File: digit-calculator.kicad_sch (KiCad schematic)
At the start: 4 parts, among them J1 Trackball, SW1 SW_SPST, U1 XIAO-ESP32-C3-SMD

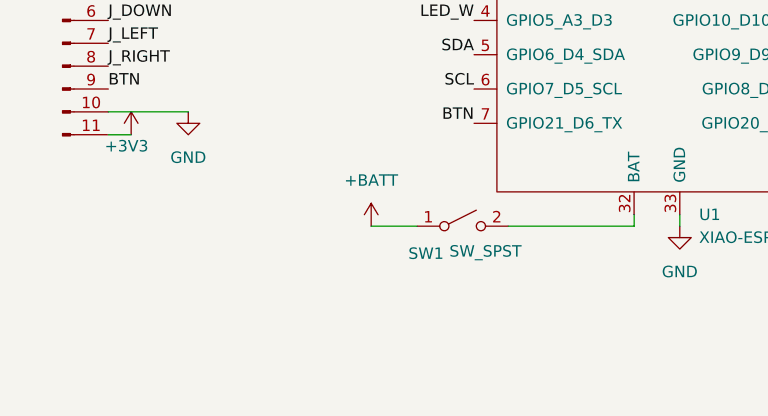
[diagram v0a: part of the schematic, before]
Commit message: Add battery connector
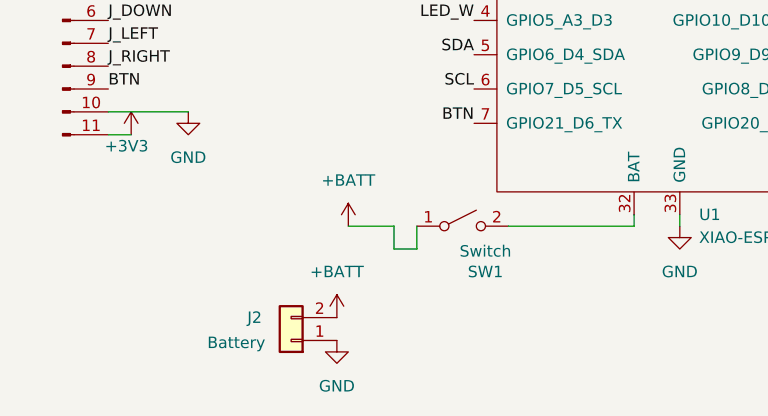
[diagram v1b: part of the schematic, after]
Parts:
- added J2: Battery, symbol Connector_Generic:Conn_01x02
- Brd1: footprint Display:SSD1306-OLED -> Display:SSD1306-0.91-OLED-4pin-128x32
- SW1: value SW_SPST -> Switch
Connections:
- net +BATT: now also J2.2 (Pin_2)
- net GND: now also J2.1 (Pin_1)
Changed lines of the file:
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@@
+	(wire
+		(pts
+			(xy 111.76 115.57) (xy 114.3 115.57)
+		)
+		(stroke
+			(width 0)
+			(type default)
+		)
+	)
+	(wire
+		(pts
+			(xy 111.76 113.03) (xy 111.76 115.57)
+		)
+		(stroke
+			(width 0)
+			(type default)
+		)
+	)
 	(wire
 		(pts
@@
 	(wire
 		(pts
-			(xy 109.22 113.03) (xy 114.3 113.03)
+			(xy 114.3 115.57) (xy 114.3 113.03)
 		)
 		(stroke
@@
 	(wire
 		(pts
-			(xy 124.46 113.03) (xy 138.43 113.03)
+			(xy 106.68 113.03) (xy 111.76 113.03)
 		)
 		(stroke
@@
 	(wire
 		(pts
-			(xy 138.43 113.03) (xy 138.43 111.76)
+			(xy 124.46 113.03) (xy 138.43 113.03)
 		)
 		(stroke
@@
 	(wire
 		(pts
-			(xy 162.56 86.36) (xy 170.18 86.36)
+			(xy 138.43 113.03) (xy 138.43 111.76)
 		)
 		(stroke
@@
 	(wire
 		(pts
-			(xy 143.51 52.07) (xy 143.51 59.69)
+			(xy 162.56 86.36) (xy 170.18 86.36)
 		)
 		(stroke
@@
 		)
 	)
+	(wire
+		(pts
+			(xy 143.51 52.07) (xy 143.51 59.69)
+		)
+		(stroke
+			(width 0)
+			(type default)
+		)
+	)
 	(label "BTN"
 		(at 80.01 97.79 0)
@@
 			)
 		)
-		(property "Footprint" "Display:SSD1306-OLED"
+		(property "Footprint" "Display:SSD1306-0.91-OLED-4pin-128x32"
 			(at 194.31 86.36 0)
 			(effects
@@
 	)
 	(symbol
+		(lib_id "power:+BATT")
+		(at 106.68 113.03 0)
+		(unit 1)
+		(exclude_from_sim no)
+		(in_bom yes)
+		(on_board yes)
+		(dnp no)
+		(fields_autoplaced yes)
+		(property "Reference" "#PWR011"
+			(at 106.68 116.84 0)
+			(effects
+				(font
+					(size 1.27 1.27)
+				)
+				(hide yes)
+			)
+		)
+		(property "Value" "+BATT"
+			(at 106.68 107.95 0)
+			(effects
+				(font
+					(size 1.27 1.27)
+				)
+			)
+		)
+		(property "Footprint" ""
+			(at 106.68 113.03 0)
+			(effects
+				(font
+					(size 1.27 1.27)
+				)
+				(hide yes)
+			)
+		)
+		(property "Datasheet" ""
+			(at 106.68 113.03 0)
+			(effects
+				(font
+					(size 1.27 1.27)
+				)
+				(hide yes)
+			)
+		)
+		(property "Description" "Power symbol creates a global label with name \"+BATT\""
+			(at 106.68 113.03 0)
+			(effects
+				(font
+					(size 1.27 1.27)
+				)
+				(hide yes)
+			)
+		)
+		(pin "1"
+		)
+		(instances
+			(project "digit-calculator"
+				(path "/6cc797f4-54df-4b9b-886e-e7e62ef7b713"
+					(reference "#PWR011")
+					(unit 1)
+				)
+			)
+		)
+	)
+	(symbol
+		(lib_id "Connector_Generic:Conn_01x02")
+		(at 100.33 125.73 180)
+		(unit 1)
+		(exclude_from_sim no)
+		(in_bom yes)
+		(on_board yes)
+		(dnp no)
+		(property "Reference" "J2"
+			(at 96.266 123.19 0)
+			(effects
+				(font
+					(size 1.27 1.27)
+				)
+			)
+		)
+		(property "Value" "Battery"
+			(at 94.234 125.984 0)
+			(effects
+				(font
+					(size 1.27 1.27)
+				)
+			)
+		)
+		(property "Footprint" ""
+			(at 100.33 125.73 0)
+			(effects
+				(font
+					(size 1.27 1.27)
+				)
+				(hide yes)
+			)
+		)
+		(property "Datasheet" "~"
+			(at 100.33 125.73 0)
+			(effects
+				(font
+					(size 1.27 1.27)
+				)
+				(hide yes)
+			)
+		)
+		(property "Description" "Generic connector, single row, 01x02, script generated (kicad-library-utils/schlib/autogen/connector/)"
+			(at 100.33 125.73 0)
+			(effects
+				(font
+					(size 1.27 1.27)
+				)
+				(hide yes)
+			)
+		)
+		(pin "1"
+		)
+		(pin "2"
+		)
+		(instances
+			(project ""
+				(path "/6cc797f4-54df-4b9b-886e-e7e62ef7b713"
+					(reference "J2")
+					(unit 1)
+				)
+			)
+		)
+	)
+	(symbol
 		(lib_id "power:+3V3")
 		(at 170.18 86.36 0)
@@
 	(symbol
 		(lib_id "power:+BATT")
-		(at 109.22 113.03 0)
+		(at 105.41 123.19 0)
 		(unit 1)
 		(exclude_from_sim no)
@@
 		(fields_autoplaced yes)
 		(property "Reference" "#PWR09"
-			(at 109.22 116.84 0)
+			(at 105.41 127 0)
 			(effects
 				(font
@@
 		)
 		(property "Value" "+BATT"
-			(at 109.22 107.95 0)
+			(at 105.41 118.11 0)
 			(effects
 				(font
@@
 		)
 		(property "Footprint" ""
-			(at 109.22 113.03 0)
+			(at 105.41 123.19 0)
 			(effects
 				(font
@@
 		)
 		(property "Datasheet" ""
-			(at 109.22 113.03 0)
+			(at 105.41 123.19 0)
 			(effects
 				(font
@@
 		)
 		(property "Description" "Power symbol creates a global label with name \"+BATT\""
-			(at 109.22 113.03 0)
-			(effects
-				(font
-					(size 1.27 1.27)
-				)
-				(hide yes)
-			)
-		)
-		(pin "1"
-		)
-		(instances
-			(project ""
+			(at 105.41 123.19 0)
+			(effects
+				(font
+					(size 1.27 1.27)
+				)
+				(hide yes)
+			)
+		)
+		(pin "1"
+		)
+		(instances
+			(project "digit-calculator"
 				(path "/6cc797f4-54df-4b9b-886e-e7e62ef7b713"
 					(reference "#PWR09")
@@
 		(dnp no)
 		(property "Reference" "SW1"
-			(at 115.316 116.078 0)
-			(effects
-				(font
-					(size 1.27 1.27)
-				)
-			)
-		)
-		(property "Value" "SW_SPST"
+			(at 121.92 118.11 0)
+			(effects
+				(font
+					(size 1.27 1.27)
+				)
+			)
+		)
+		(property "Value" "Switch"
 			(at 121.92 115.824 0)
 			(effects
@@
 					(unit 1)
 				)
+			)
+		)
+	)
+	(symbol
+		(lib_id "power:GND")
+		(at 105.41 125.73 0)
+		(unit 1)
+		(exclude_from_sim no)
+		(in_bom yes)
+		(on_board yes)
+		(dnp no)
+		(fields_autoplaced yes)
+		(property "Reference" "#PWR010"
+			(at 105.41 132.08 0)
+			(effects
+				(font
+					(size 1.27 1.27)
+				)
+				(hide yes)
+			)
+		)
+		(property "Value" "GND"
+			(at 105.41 130.81 0)
+			(effects
+				(font
+					(size 1.27 1.27)
+				)
+			)
+		)
+		(property "Footprint" ""
+			(at 105.41 125.73 0)
+			(effects
+				(font
+					(size 1.27 1.27)
+				)
+				(hide yes)
+			)
+		)
+		(property "Datasheet" ""
+			(at 105.41 125.73 0)
+			(effects
+				(font
+					(size 1.27 1.27)
+				)
+				(hide yes)
+			)
+		)
+		(property "Description" "Power symbol creates a global label with name \"GND\" , ground"
+			(at 105.41 125.73 0)
+			(effects
+				(font
+					(size 1.27 1.27)
+				)
+				(hide yes)
+			)
+		)
+		(pin "1"
+		)
+		(instances
+			(project "digit-calculator"
+				(path "/6cc797f4-54df-4b9b-886e-e7e62ef7b713"
+					(reference "#PWR010")
+					(unit 1)
+				)

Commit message: initial pcb design
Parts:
- J2: footprint (none) -> Connector_PinHeader_2.54mm:PinHeader_1x02_P2.54mm_Vertical
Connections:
- net J_DOWN: now also U1.9 (GPIO8_D8_SCK); no longer U1.10 (GPIO9_D9_MISO)
- net J_LEFT: now also U1.10 (GPIO9_D9_MISO); no longer U1.9 (GPIO8_D8_SCK)
- net J_RIGHT: now also U1.11 (GPIO10_D10_MOSI); no longer U1.8 (GPIO20_D7_RX)
- net J_UP: now also U1.8 (GPIO20_D7_RX); no longer U1.11 (GPIO10_D10_MOSI)
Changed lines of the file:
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@@
 	)
 	(label "J_RIGHT"
-		(at 162.56 101.6 0)
+		(at 162.56 90.17 0)
 		(effects
 			(font
@@
 	)
 	(label "J_LEFT"
-		(at 162.56 97.79 0)
+		(at 162.56 93.98 0)
 		(effects
 			(font
@@
 	)
 	(label "J_UP"
-		(at 162.56 90.17 0)
+		(at 162.56 101.6 0)
 		(effects
 			(font
@@
 	)
 	(label "J_DOWN"
-		(at 162.56 93.98 0)
+		(at 162.56 97.79 0)
 		(effects
 			(font
@@
 			)
 		)
-		(property "Footprint" ""
+		(property "Footprint" "Connector_PinHeader_2.54mm:PinHeader_1x02_P2.54mm_Vertical"
 			(at 100.33 125.73 0)
 			(effects

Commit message: switch to a bigger OLED, add more silkscreen, reroute everything, resize the board
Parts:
- Brd1: footprint Display:SSD1306-0.91-OLED-4pin-128x32 -> Display:SSD1306-OLED
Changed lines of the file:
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@@
 			)
 		)
-		(property "Footprint" "Display:SSD1306-0.91-OLED-4pin-128x32"
+		(property "Footprint" "Display:SSD1306-OLED"
 			(at 194.31 86.36 0)
 			(effects
